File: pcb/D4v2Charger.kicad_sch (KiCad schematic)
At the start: 17 parts, among them J1 Conn_01x02_Pin, U1 BQ25185DLHR

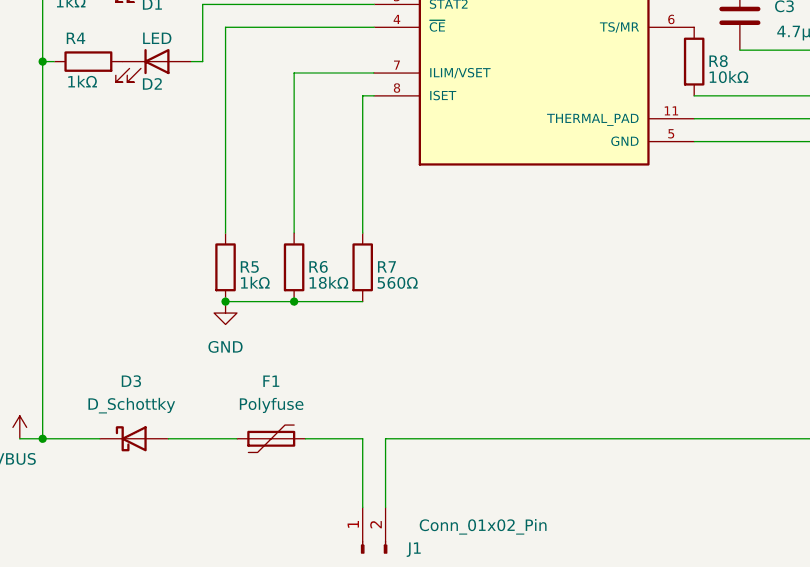
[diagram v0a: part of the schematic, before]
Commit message: create diode 3dModel
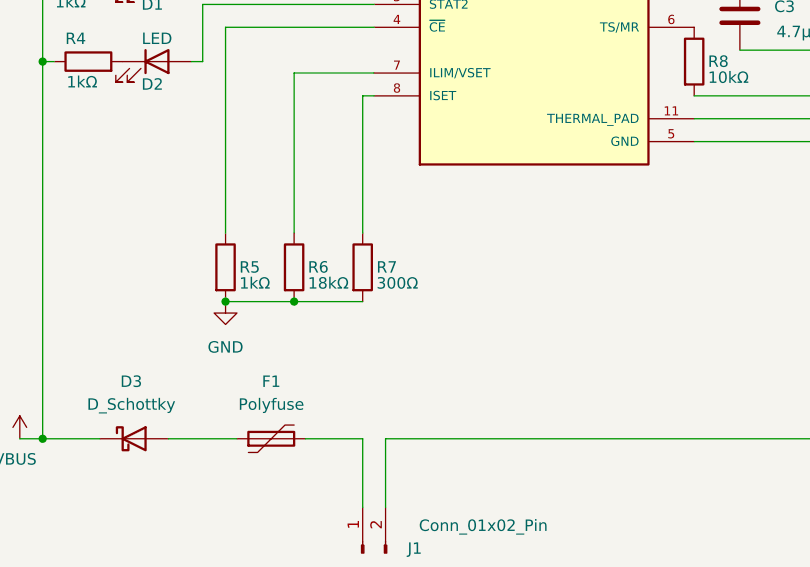
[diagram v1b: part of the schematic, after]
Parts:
- R7: value 560Ω -> 300Ω
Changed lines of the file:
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@@
 			)
 		)
-		(property "Value" "560Ω"
+		(property "Value" "300Ω"
 			(at 133.604 104.648 0)
 			(effects

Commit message: 3dFootprint updates
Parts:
- D3: value D_Schottky -> 60V, 1A cont.
- F1: value Polyfuse -> 1A hold, 2A trip
- R7: value 300Ω -> 390Ω
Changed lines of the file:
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@@
+	)
+	(junction
+		(at 201.93 88.9)
+		(diameter 0)
+		(color 0 0 0 0)
 	)
 	(junction
@@
 	)
 	(junction
-		(at 191.77 121.92)
-		(diameter 0)
-		(color 0 0 0 0)
-	)
-	(junction
-		(at 191.77 88.9)
-		(diameter 0)
-		(color 0 0 0 0)
-	)
-	(junction
 		(at 124.46 106.68)
 		(diameter 0)
@@
 	)
 	(junction
-		(at 151.13 49.53)
+		(at 130.81 66.04)
 		(diameter 0)
 		(color 0 0 0 0)
 	)
 	(junction
-		(at 130.81 66.04)
+		(at 201.93 86.36)
 		(diameter 0)
 		(color 0 0 0 0)
@@
 	(wire
 		(pts
-			(xy 191.77 86.36) (xy 191.77 88.9)
-		)
-		(stroke
-			(width 0)
-			(type default)
-		)
-	)
-	(wire
-		(pts
 			(xy 93.98 121.92) (xy 96.52 121.92)
 		)
@@
 	(wire
 		(pts
+			(xy 201.93 88.9) (xy 201.93 86.36)
+		)
+		(stroke
+			(width 0)
+			(type default)
+		)
+	)
+	(wire
+		(pts
 			(xy 116.84 106.68) (xy 124.46 106.68)
 		)
@@
 	(wire
 		(pts
-			(xy 130.81 58.42) (xy 130.81 49.53)
+			(xy 130.81 58.42) (xy 130.81 48.26)
 		)
 		(stroke
@@
 	(wire
 		(pts
-			(xy 134.62 121.92) (xy 191.77 121.92)
+			(xy 134.62 121.92) (xy 163.83 121.92)
 		)
 		(stroke
@@
 	(wire
 		(pts
+			(xy 201.93 86.36) (xy 201.93 83.82)
+		)
+		(stroke
+			(width 0)
+			(type default)
+		)
+	)
+	(wire
+		(pts
 			(xy 125.73 121.92) (xy 132.08 121.92)
 		)
@@
 	(wire
 		(pts
+			(xy 201.93 90.17) (xy 201.93 88.9)
+		)
+		(stroke
+			(width 0)
+			(type default)
+		)
+	)
+	(wire
+		(pts
+			(xy 173.99 49.53) (xy 182.88 49.53)
+		)
+		(stroke
+			(width 0)
+			(type default)
+		)
+	)
+	(wire
+		(pts
 			(xy 201.93 57.15) (xy 201.93 71.12)
 		)
@@
 	(wire
 		(pts
-			(xy 191.77 88.9) (xy 191.77 121.92)
-		)
-		(stroke
-			(width 0)
-			(type default)
-		)
-	)
-	(wire
-		(pts
-			(xy 151.13 49.53) (xy 173.99 49.53)
-		)
-		(stroke
-			(width 0)
-			(type default)
-		)
-	)
-	(wire
-		(pts
-			(xy 168.91 86.36) (xy 191.77 86.36)
+			(xy 168.91 86.36) (xy 201.93 86.36)
 		)
 		(stroke
@@
 	(wire
 		(pts
-			(xy 130.81 49.53) (xy 151.13 49.53)
-		)
-		(stroke
-			(width 0)
-			(type default)
-		)
-	)
-	(wire
-		(pts
-			(xy 168.91 88.9) (xy 191.77 88.9)
+			(xy 130.81 48.26) (xy 121.92 48.26)
+		)
+		(stroke
+			(width 0)
+			(type default)
+		)
+	)
+	(wire
+		(pts
+			(xy 168.91 88.9) (xy 201.93 88.9)
 		)
 		(stroke
@@
 	)
 	(symbol
+		(lib_id "power:GND")
+		(at 182.88 49.53 0)
+		(unit 1)
+		(exclude_from_sim no)
+		(in_bom yes)
+		(on_board yes)
+		(dnp no)
+		(fields_autoplaced yes)
+		(property "Reference" "#PWR06"
+			(at 182.88 55.88 0)
+			(effects
+				(font
+					(size 1.27 1.27)
+				)
+				(hide yes)
+			)
+		)
+		(property "Value" "GND"
+			(at 182.88 54.61 0)
+			(effects
+				(font
+					(size 1.27 1.27)
+				)
+			)
+		)
+		(property "Footprint" ""
+			(at 182.88 49.53 0)
+			(effects
+				(font
+					(size 1.27 1.27)
+				)
+				(hide yes)
+			)
+		)
+		(property "Datasheet" ""
+			(at 182.88 49.53 0)
+			(effects
+				(font
+					(size 1.27 1.27)
+				)
+				(hide yes)
+			)
+		)
+		(property "Description" "Power symbol creates a global label with name \"GND\" , ground"
+			(at 182.88 49.53 0)
+			(effects
+				(font
+					(size 1.27 1.27)
+				)
+				(hide yes)
+			)
+		)
+		(pin "1"
+		)
+		(instances
+			(project "D4v2Charger"
+				(path "/88573ec5-2eb3-489f-b9be-0922d5590a50"
+					(reference "#PWR06")
+					(unit 1)
+				)
+			)
+		)
+	)
+	(symbol
 		(lib_id "Device:R")
 		(at 101.6 71.12 90)
@@
 	(symbol
 		(lib_id "power:GND")
-		(at 151.13 49.53 0)
+		(at 121.92 48.26 0)
 		(unit 1)
 		(exclude_from_sim no)
@@
 		(fields_autoplaced yes)
 		(property "Reference" "#PWR03"
-			(at 151.13 55.88 0)
+			(at 121.92 54.61 0)
 			(effects
 				(font
@@
 		)
 		(property "Value" "GND"
-			(at 151.13 54.61 0)
+			(at 121.92 53.34 0)
 			(effects
 				(font
@@
 		)
 		(property "Footprint" ""
-			(at 151.13 49.53 0)
+			(at 121.92 48.26 0)
 			(effects
 				(font
@@
 		)
 		(property "Datasheet" ""
-			(at 151.13 49.53 0)
+			(at 121.92 48.26 0)
 			(effects
 				(font
@@
 		)
 		(property "Description" "Power symbol creates a global label with name \"GND\" , ground"
-			(at 151.13 49.53 0)
+			(at 121.92 48.26 0)
 			(effects
 				(font
@@
 			)
 		)
-		(property "Value" "300Ω"
+		(property "Value" "390Ω"
 			(at 133.604 104.648 0)
 			(effects
@@
 			)
 		)
-		(property "Value" "Polyfuse"
+		(property "Value" "1A hold, 2A trip"
 			(at 121.92 118.11 90)
 			(effects
@@
 	(symbol
 		(lib_id "power:GND")
-		(at 201.93 83.82 0)
+		(at 201.93 90.17 0)
 		(unit 1)
 		(exclude_from_sim no)
@@
 		(fields_autoplaced yes)
 		(property "Reference" "#PWR04"
+			(at 201.93 96.52 0)
+			(effects
+				(font
+					(size 1.27 1.27)
+				)
+				(hide yes)
+			)
+		)
+		(property "Value" "GND"
+			(at 201.93 95.25 0)
+			(effects
+				(font
+					(size 1.27 1.27)
+				)
+			)
+		)
+		(property "Footprint" ""
 			(at 201.93 90.17 0)
 			(effects
@@
 			)
 		)
-		(property "Value" "GND"
-			(at 201.93 88.9 0)
-			(effects
-				(font
-					(size 1.27 1.27)
-				)
-			)
-		)
-		(property "Footprint" ""
-			(at 201.93 83.82 0)
-			(effects
-				(font
-					(size 1.27 1.27)
-				)
-				(hide yes)
-			)
-		)
 		(property "Datasheet" ""
-			(at 201.93 83.82 0)
+			(at 201.93 90.17 0)
 			(effects
 				(font
@@
 		)
 		(property "Description" "Power symbol creates a global label with name \"GND\" , ground"
-			(at 201.93 83.82 0)
+			(at 201.93 90.17 0)
 			(effects
 				(font
@@
 	(symbol
 		(lib_id "power:GND")
-		(at 191.77 121.92 0)
+		(at 163.83 121.92 0)
 		(unit 1)
 		(exclude_from_sim no)
@@
 		(fields_autoplaced yes)
 		(property "Reference" "#PWR01"
-			(at 191.77 128.27 0)
+			(at 163.83 128.27 0)
 			(effects
 				(font
@@
 		)
 		(property "Value" "GND"
-			(at 191.77 127 0)
+			(at 163.83 127 0)
 			(effects
 				(font
@@
 		)
 		(property "Footprint" ""
-			(at 191.77 121.92 0)
+			(at 163.83 121.92 0)
 			(effects
 				(font
@@
 		)
 		(property "Datasheet" ""
-			(at 191.77 121.92 0)
+			(at 163.83 121.92 0)
 			(effects
 				(font
@@
 		)
 		(property "Description" "Power symbol creates a global label with name \"GND\" , ground"
-			(at 191.77 121.92 0)
+			(at 163.83 121.92 0)
 			(effects
 				(font
@@
 			)
 		)
-		(property "Value" "D_Schottky"
+		(property "Value" "60V, 1A cont."
 			(at 106.3625 118.11 0)
 			(effects

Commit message: update pcb with spring contact for battery +
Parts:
- TP1: footprint TestPoint:TestPoint_Pad_D3.0mm -> Custom_TestPoints:TestPoint_Pad_D6.0mm_spring
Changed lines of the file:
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@@
 			)
 		)
-		(property "Footprint" "TestPoint:TestPoint_Pad_D3.0mm"
+		(property "Footprint" "Custom_TestPoints:TestPoint_Pad_D6.0mm_spring"
 			(at 207.01 57.15 0)
 			(effects

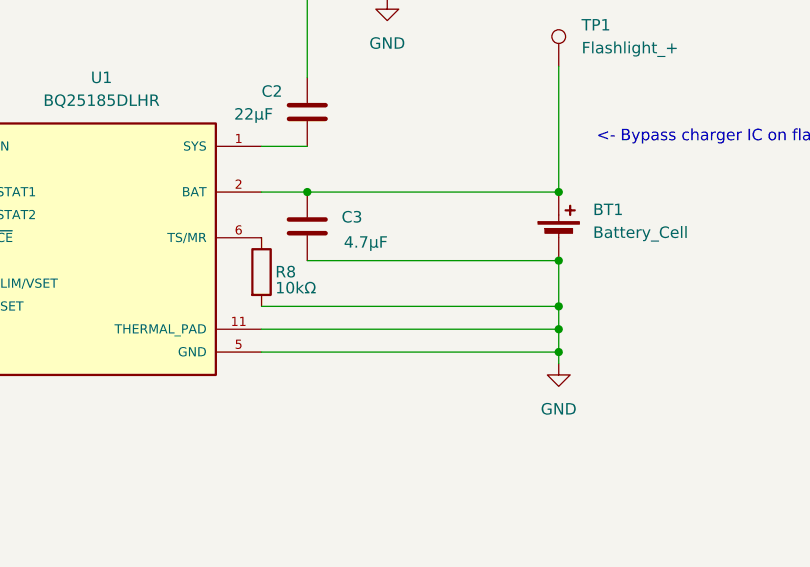
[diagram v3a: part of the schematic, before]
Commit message: add ntcg thremistor & drc resolve
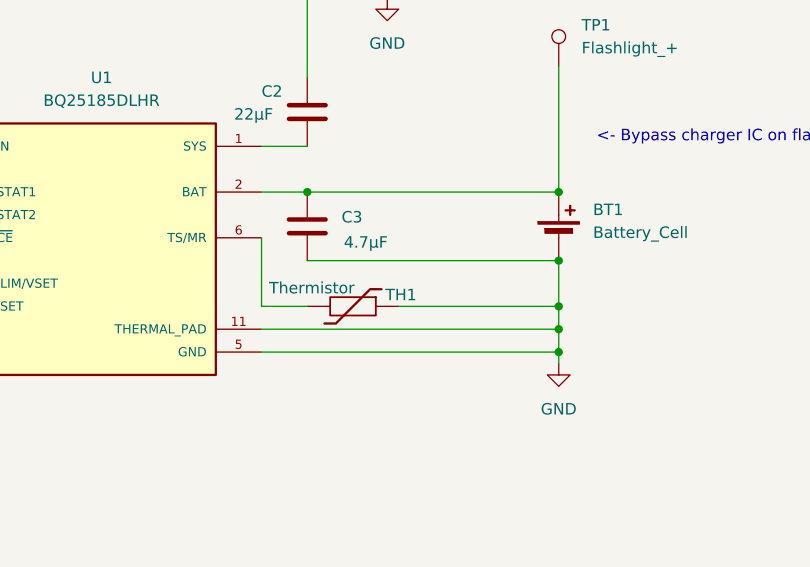
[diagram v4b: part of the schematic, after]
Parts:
- removed R8: 10kΩ, Resistor_SMD:R_0402_1005Metric, symbol Device:R
- added TH1: Thermistor, NTCG103JF103FT1:THERM_NTCG103JF103FT1, symbol Device:Thermistor
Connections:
- net GND: now also TH1.1
- net at U1.6 (TS/MR): now also TH1.2
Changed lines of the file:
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@@
+	)
+	(junction
+		(at 201.93 83.82)
+		(diameter 0)
+		(color 0 0 0 0)
 	)
 	(junction
@@
 	)
 	(junction
-		(at 201.93 83.82)
-		(diameter 0)
-		(color 0 0 0 0)
-	)
-	(junction
 		(at 96.52 80.01)
 		(diameter 0)
@@
 	(wire
 		(pts
+			(xy 168.91 83.82) (xy 173.99 83.82)
+		)
+		(stroke
+			(width 0)
+			(type default)
+		)
+	)
+	(wire
+		(pts
 			(xy 93.98 121.92) (xy 96.52 121.92)
 		)
@@
 	(wire
 		(pts
+			(xy 201.93 83.82) (xy 201.93 86.36)
+		)
+		(stroke
+			(width 0)
+			(type default)
+		)
+	)
+	(wire
+		(pts
 			(xy 110.49 121.92) (xy 118.11 121.92)
 		)
@@
 	(wire
 		(pts
-			(xy 168.91 83.82) (xy 201.93 83.82)
-		)
-		(stroke
-			(width 0)
-			(type default)
-		)
-	)
-	(wire
-		(pts
 			(xy 173.99 78.74) (xy 201.93 78.74)
 		)
@@
 	(wire
 		(pts
+			(xy 168.91 76.2) (xy 168.91 83.82)
+		)
+		(stroke
+			(width 0)
+			(type default)
+		)
+	)
+	(wire
+		(pts
 			(xy 113.03 80.01) (xy 114.3 80.01)
 		)
@@
 	(wire
 		(pts
-			(xy 201.93 86.36) (xy 201.93 83.82)
-		)
-		(stroke
-			(width 0)
-			(type default)
-		)
-	)
-	(wire
-		(pts
 			(xy 125.73 121.92) (xy 132.08 121.92)
 		)
@@
 		(pts
 			(xy 201.93 57.15) (xy 201.93 71.12)
+		)
+		(stroke
+			(width 0)
+			(type default)
+		)
+	)
+	(wire
+		(pts
+			(xy 184.15 83.82) (xy 201.93 83.82)
 		)
 		(stroke
@@
 	)
 	(symbol
+		(lib_id "Device:Thermistor")
+		(at 179.07 83.82 270)
+		(unit 1)
+		(exclude_from_sim no)
+		(in_bom yes)
+		(on_board yes)
+		(dnp no)
+		(property "Reference" "TH1"
+			(at 184.404 82.55 90)
+			(effects
+				(font
+					(size 1.27 1.27)
+				)
+			)
+		)
+		(property "Value" "Thermistor"
+			(at 174.498 81.788 90)
+			(effects
+				(font
+					(size 1.27 1.27)
+				)
+			)
+		)
+		(property "Footprint" "NTCG103JF103FT1:THERM_NTCG103JF103FT1"
+			(at 179.07 83.82 0)
+			(effects
+				(font
+					(size 1.27 1.27)
+				)
+				(hide yes)
+			)
+		)
+		(property "Datasheet" "~"
+			(at 179.07 83.82 0)
+			(effects
+				(font
+					(size 1.27 1.27)
+				)
+				(hide yes)
+			)
+		)
+		(property "Description" "Temperature dependent resistor"
+			(at 179.07 83.82 0)
+			(effects
+				(font
+					(size 1.27 1.27)
+				)
+				(hide yes)
+			)
+		)
+		(pin "1"
+		)
+		(pin "2"
+		)
+		(instances
+			(project ""
+				(path "/88573ec5-2eb3-489f-b9be-0922d5590a50"
+					(reference "TH1")
+					(unit 1)
+				)
+			)
+		)
+	)
+	(symbol
 		(lib_id "power:GND")
 		(at 116.84 106.68 0)
@@
 					(unit 1)
 				)
-			)
-		)
-	)
-	(symbol
-		(lib_id "Device:R")
-		(at 168.91 80.01 0)
-		(unit 1)
-		(exclude_from_sim no)
-		(in_bom yes)
-		(on_board yes)
-		(dnp no)
-		(property "Reference" "R8"
-			(at 170.434 80.01 0)
-			(effects
-				(font
-					(size 1.27 1.27)
-				)
-				(justify left)
-			)
-		)
-		(property "Value" "10kΩ"
-			(at 170.434 81.788 0)
-			(effects
-				(font
-					(size 1.27 1.27)
-				)
-				(justify left)
-			)
-		)
-		(property "Footprint" "Resistor_SMD:R_0402_1005Metric"
-			(at 167.132 80.01 90)
-			(effects
-				(font
-					(size 1.27 1.27)
-				)
-				(hide yes)
-			)
-		)
-		(property "Datasheet" "~"
-			(at 168.91 80.01 0)
-			(effects
-				(font
-					(size 1.27 1.27)
-				)
-				(hide yes)
-			)
-		)
-		(property "Description" "Resistor"
-			(at 168.91 80.01 0)
-			(effects
-				(font
-					(size 1.27 1.27)
-				)
-				(hide yes)
-			)
-		)
-		(pin "1"
-		)
-		(pin "2"
-		)
-		(instances
-			(project "D4v2Charger"
-				(path "/88573ec5-2eb3-489f-b9be-0922d5590a50"
-					(reference "R8")
-					(unit 1)
-				)
